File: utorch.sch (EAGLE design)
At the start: 24 parts, among them IC1 LTC4062, IC2 LTC3454, U1 2N7002BKW, X1 USB-MICROB

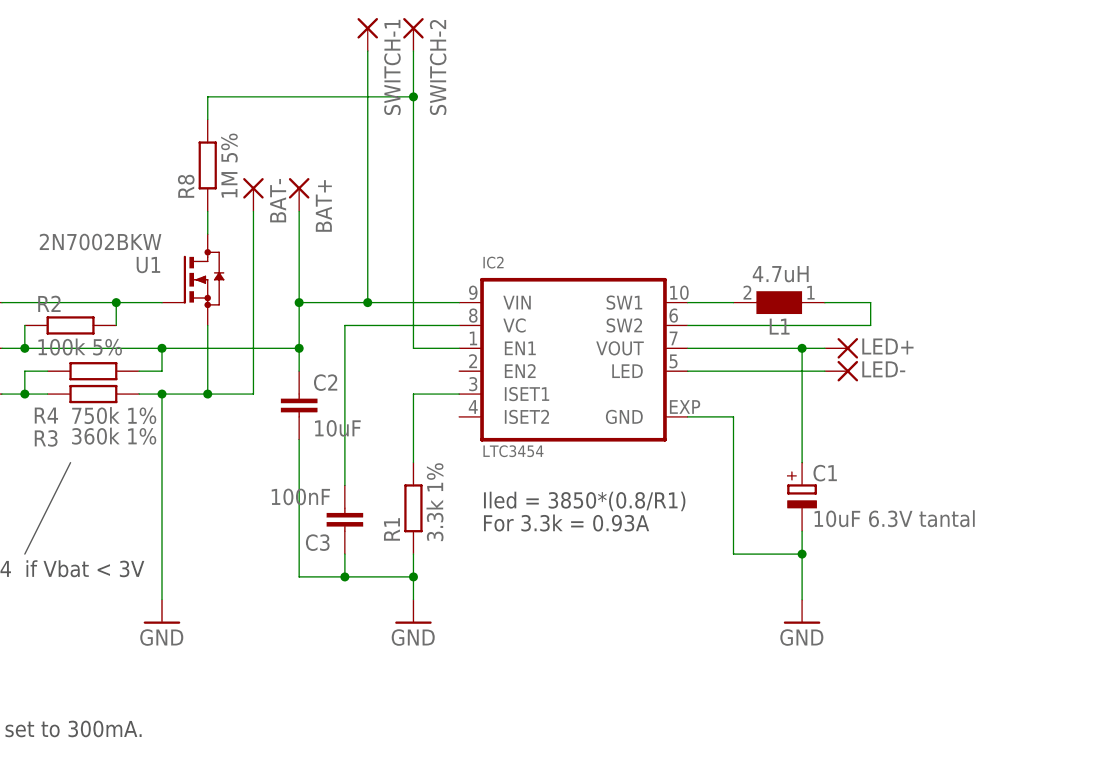
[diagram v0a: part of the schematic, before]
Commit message: Fixed on/off logic
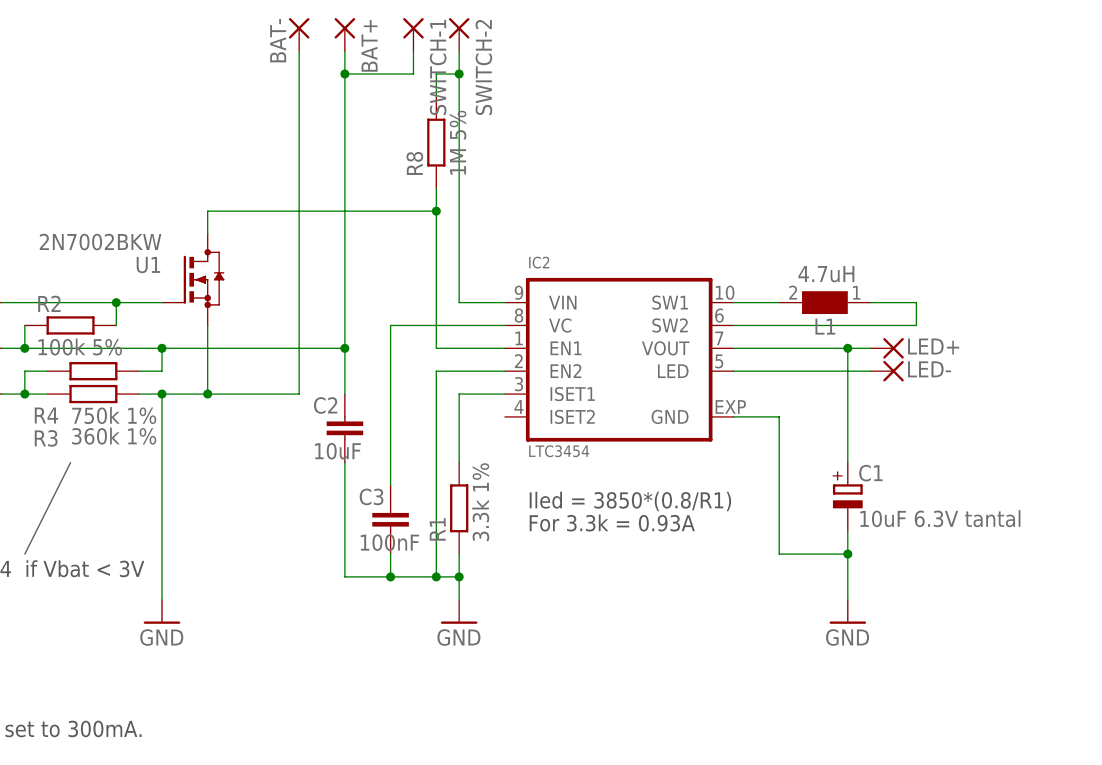
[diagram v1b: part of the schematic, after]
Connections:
- removed net N$15: BAT+.P, C2.1, IC1.BAT, IC2.VIN, R2.1, R4.1, SWITCH-1.P
- new net BAT+: BAT+.P, C2.1, IC1.BAT, R2.1, R4.1, SWITCH-1.P
- net GND: now also IC2.EN2
- net N$16: now also IC2.EN1
- net N$7: now also IC2.VIN; no longer IC2.EN1
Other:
- moved on the sheet: BAT+, BAT-, C1, C2, C3, IC2, L1, LED+, LED-, R1, R8, SWITCH-1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

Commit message: Fixed ltc4062 enable pin...
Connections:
- net N$14: no longer IC1.!EN
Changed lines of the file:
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@@
 <junction x="60.96" y="111.76"/>
 <pinref part="X1" gate="G$1" pin="VBUS"/>
-<pinref part="IC1" gate="G$1" pin="!EN"/>
-<wire x1="88.9" y1="101.6" x2="66.04" y2="101.6" width="0.1524" layer="91"/>
-<wire x1="66.04" y1="101.6" x2="66.04" y2="106.68" width="0.1524" layer="91"/>
 <junction x="66.04" y="111.76"/>
 <pinref part="CHG" gate="G$1" pin="A"/>
 <wire x1="66.04" y1="106.68" x2="66.04" y2="111.76" width="0.1524" layer="91"/>
 <wire x1="66.04" y1="106.68" x2="71.12" y2="106.68" width="0.1524" layer="91"/>
-<junction x="66.04" y="106.68"/>
 <pinref part="IC1" gate="G$1" pin="!C/5"/>
 <wire x1="88.9" y1="109.22" x2="83.82" y2="109.22" width="0.1524" layer="91"/>

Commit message: inital update
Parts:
- removed CHG: (no value), adl_lib_001:LEDCHIP-LED0603
- removed R2: 100k 5%, adl_lib_001:R-EU_R0402
- removed R7: 560 5%, resistor:R-EU_R0402
- removed U1: 2N7002BKW, WB:2N7002BKW
- added C5: 4.7uF, rcl:C-EUC0603
- added IC3: TINY13V-10MM0, atmel:TINY13V-10MM0
- added IC4: TINY24/44/84-MU, avr-4:TINY24/44/84-MU
- added LED1, LED2, LED3, LED4: (no value), led:LEDCHIPLED_1206
- added R9: 0.05R 1%, adl_lib_001:R-EU_R0402
- added U2: LTC4150, mike-temp:LTC4150
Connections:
- removed net N$12: IC1.!CHRG, R7.1
- removed net N$13: CHG.C, R7.2
- new net N$15: BAT+.P, R9.2, U2.SENSE+
- new net N$17: C5.2, U2.CF-
- new net N$18: C5.1, U2.CF+
- new net N$19: U2.!CLR!, U2.!INT!
- new net N$22: U2.POL
- net BAT+: now also R9.1, U2.SENSE-; no longer BAT+.P, R2.1
- net GND: now also U2.GND; no longer U1.S
- net N$10: no longer R2.2, U1.G
- net N$14: no longer CHG.A
- net N$16: no longer U1.D
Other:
- moved on the sheet: BAT+, BAT-, C1, C2, C3, C4, IC1, IC2, L1, LED+, LED-, R1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

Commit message: something
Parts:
- removed IC4: TINY24/44/84-MU, avr-4:TINY24/44/84-MU
- IC3: value TINY13V-10MM0 -> TINY24/44/84; device atmel:TINY13V-10MM0 -> avr-7:TINY24/44/84
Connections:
- removed net N$22: U2.POL
- new net INT: IC3.(PCINT4/T1/SCL/USCK/ADC4)PA4, U2.!CLR!, U2.!INT!
- new net LED-ENABLE: IC2.EN1, IC3.(PCINT1/AIN0/ADC1)PA1, R8.1
- new net LOW-BAT: IC1.OUT, IC3.(PCINT2/AIN1/ADC2)PA2
- new net N$21: IC3.(PCINT11/RESET/DW)PB3, LED1.C
- new net POL: IC3.(PCINT3/T0/ADC3)PA3, U2.POL
- net BAT+: now also IC2.VIN, R8.2; no longer SWITCH-1.P
- net GND: now also IC3.GND, SWITCH-2.P
- net N$10: now also IC3.(PCINT8/XTAL1/CLKI)PB0, LED4.C; no longer IC1.OUT
- net N$15: now also U2.VDD
- net N$16: now also IC3.(PCINT9/XTAL2)PB1, LED3.C; no longer IC2.EN1, R8.1
- net N$19: now also IC3.(PCINT10/INT0/OC0A/CKOUT)PB2, LED2.C; no longer U2.!CLR!, U2.!INT!
- net N$7: now also IC3.(PCINT0/AREF/ADC0)PA0, SWITCH-1.P; no longer IC2.VIN, R8.2, SWITCH-2.P
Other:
- note added: "LOW-BAT high if Vbat < 3V"
- note added: "LTC3454 - 0uA"
- note added: "LTC4062 - 3.5uA"
- note added: "LTC4150 - 1.5uA"
- note removed: "Disables LTC3454 if Vbat < 3V"
